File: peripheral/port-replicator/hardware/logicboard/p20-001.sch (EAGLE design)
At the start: 26 parts, among them IC11 74ALS04N, J0 DC9V, J11 AUDIO_JACK_3.5MM_PTH, J12 AUDIO_JACK_3.5MM_PTH, J13 AUDIO_JACK_3.5MM_PTH, J14 AUDIO_JACK_3.5MM_PTH, J7 DIN5, J8 DIN5, J9 DIN5, X0 MKDSN1,5/2-5,08

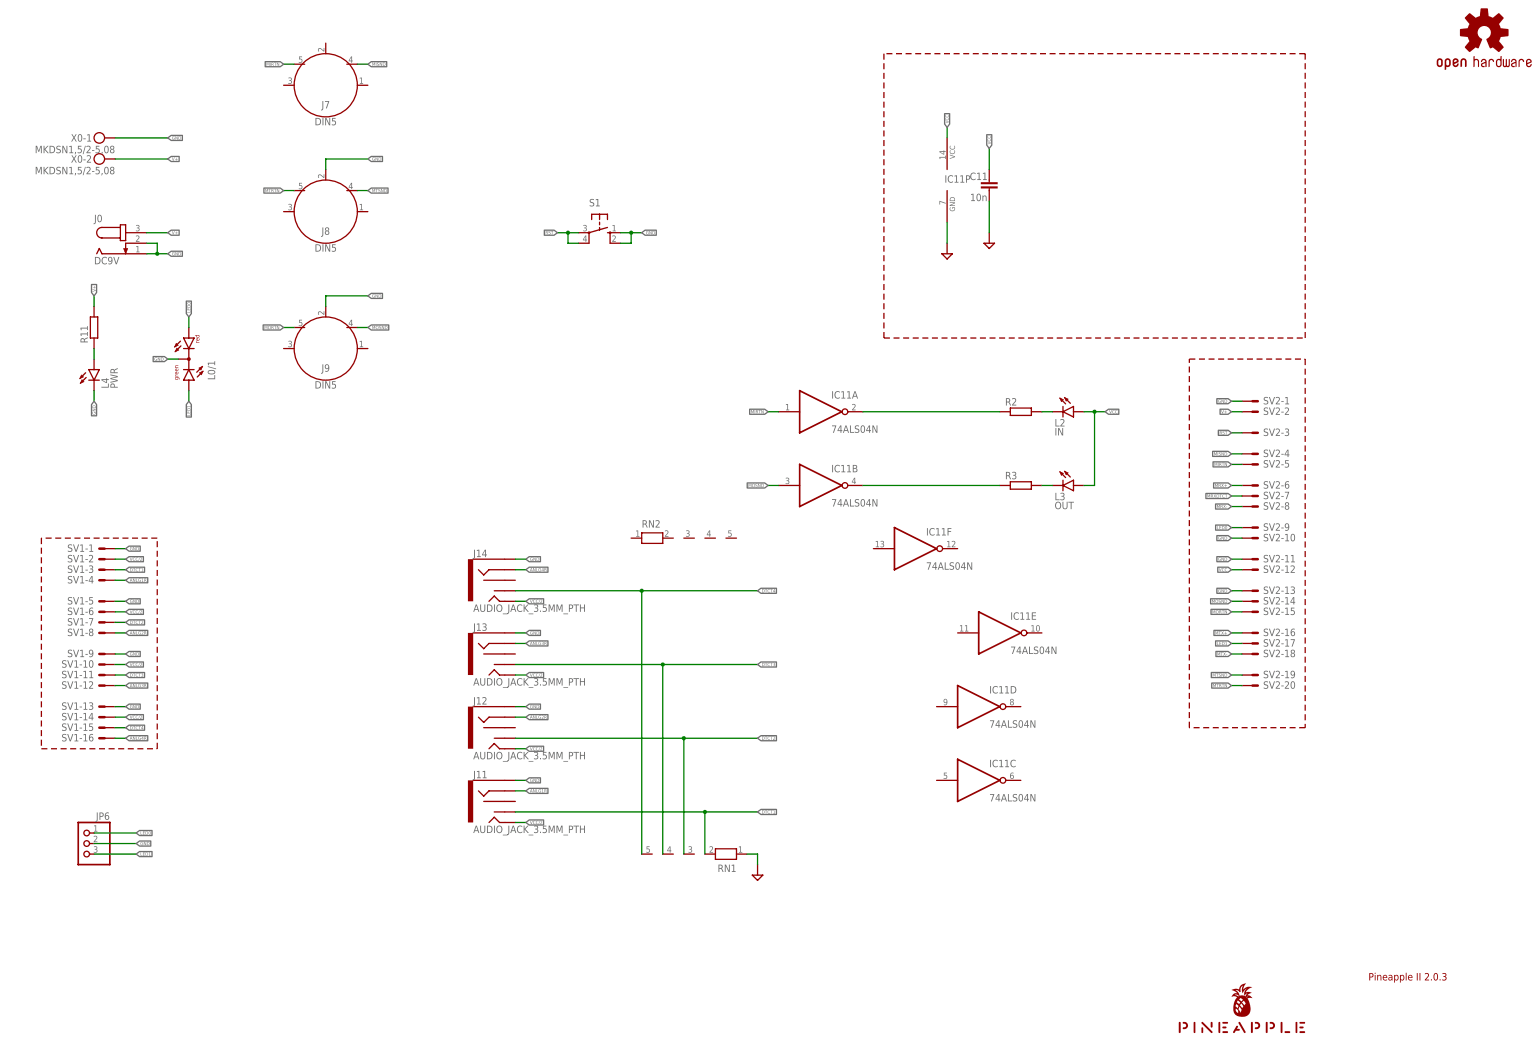
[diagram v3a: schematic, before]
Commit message: LED0->LED1, LED1->LED2, LED4->LED0.
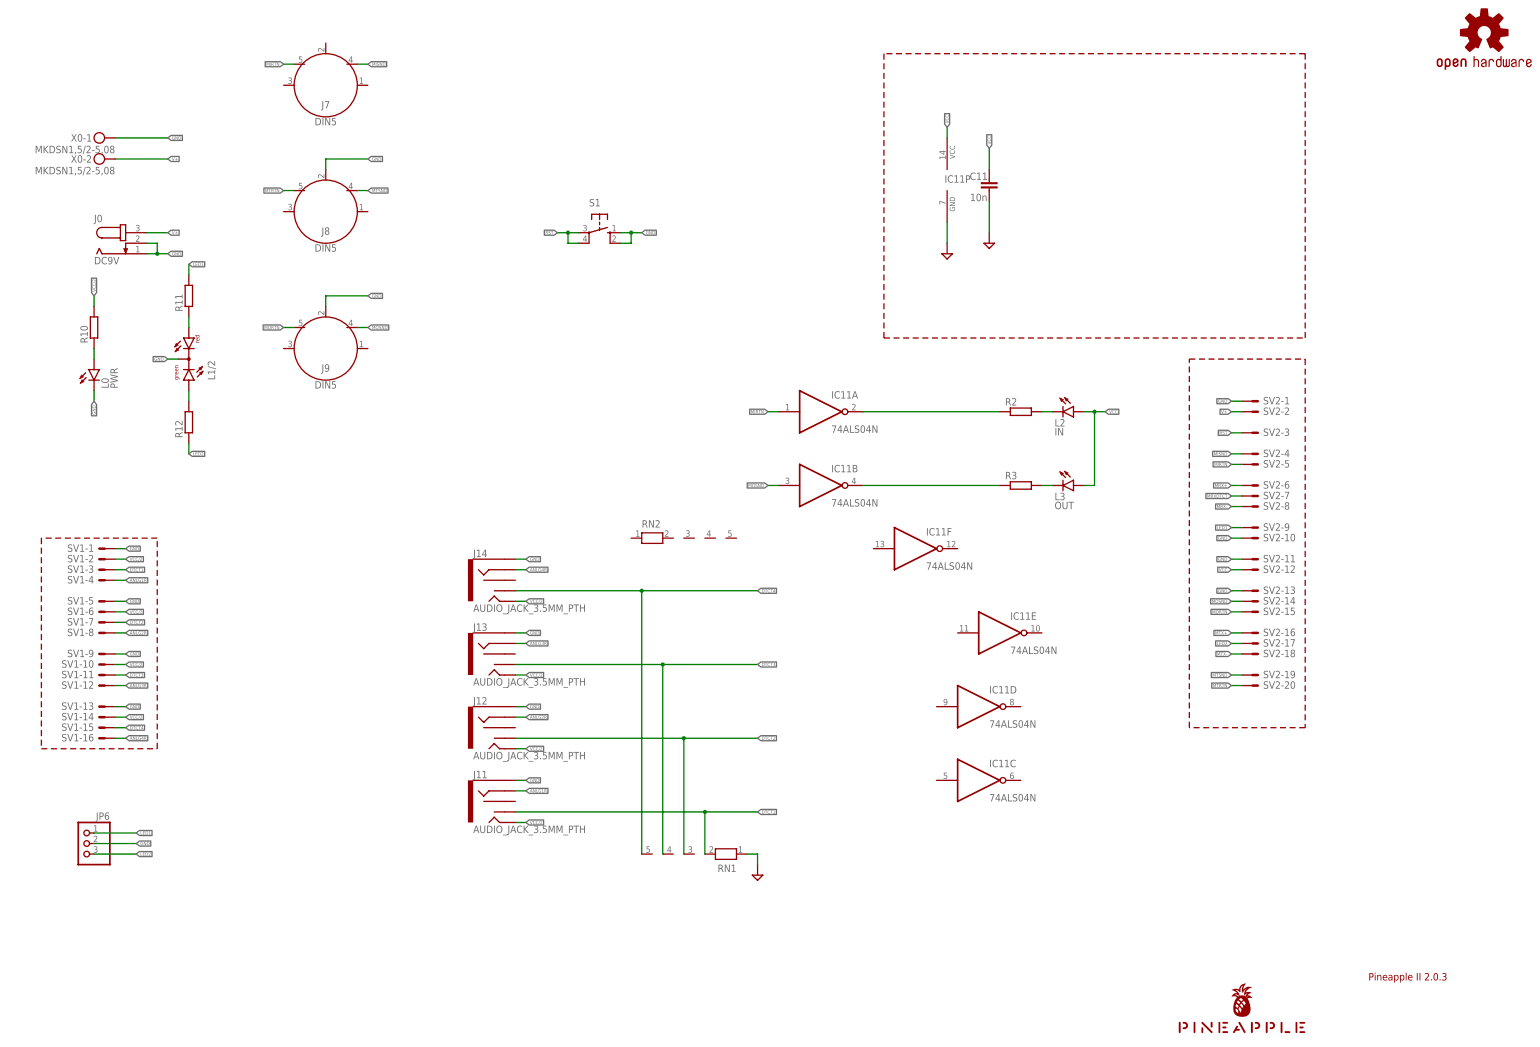
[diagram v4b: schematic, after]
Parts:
- added R10, R12: (no value), rcl:R-EU_0204/5
- renumbered L0/1 to L1/2, L4 to L0
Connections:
- removed net LED0: JP6.1, L1/2.AR, SV2-9.S
- new net LED2: JP6.3, R12.1, SV2-17.S
- new net N$3: L1/2.AR, R11.1
- new net N$5: L1/2.AG, R12.2
- net LED1: now also JP6.1, R11.2, SV2-9.S; no longer JP6.3, L1/2.AG, SV2-17.S
- net LEDPWR: now also R10.1; no longer R11.1
- net V+: no longer R11.2
- net VCC/2: now also R10.2
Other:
- moved on the sheet: R11
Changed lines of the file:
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@@
 <part name="J14" library="SparkFun-Connectors" library_urn="urn:adsk.eagle:library:513" deviceset="AUDIO_JACK_3.5MM" device="_PTH" package3d_urn="urn:adsk.eagle:package:37997/1"/>
 <part name="IC11" library="74xx-us" library_urn="urn:adsk.eagle:library:88" deviceset="74*04" device="N" package3d_urn="urn:adsk.eagle:package:16407/2" technology="ALS" value="74ALS04N"/>
-<part name="R11" library="rcl" library_urn="urn:adsk.eagle:library:334" deviceset="R-EU_" device="0204/5" package3d_urn="urn:adsk.eagle:package:23488/1"/>
+<part name="R10" library="rcl" library_urn="urn:adsk.eagle:library:334" deviceset="R-EU_" device="0204/5" package3d_urn="urn:adsk.eagle:package:23488/1"/>
 <part name="R2" library="rcl" library_urn="urn:adsk.eagle:library:334" deviceset="R-EU_" device="0204/5" package3d_urn="urn:adsk.eagle:package:23488/1"/>
-<part name="L4" library="led" library_urn="urn:adsk.eagle:library:259" deviceset="LED" device="3MM" package3d_urn="urn:adsk.eagle:package:15797/1" value="PWR"/>
+<part name="L0" library="led" library_urn="urn:adsk.eagle:library:259" deviceset="LED" device="3MM" package3d_urn="urn:adsk.eagle:package:15797/1" value="PWR"/>
 <part name="L2" library="led" library_urn="urn:adsk.eagle:library:259" deviceset="LED" device="3MM" package3d_urn="urn:adsk.eagle:package:15797/1" value="IN"/>
 <part name="L3" library="led" library_urn="urn:adsk.eagle:library:259" deviceset="LED" device="3MM" package3d_urn="urn:adsk.eagle:package:15797/1" value="OUT"/>
@@
 <part name="S1" library="switch-omron" library_urn="urn:adsk.eagle:library:377" deviceset="10-XX" device="" package3d_urn="urn:adsk.eagle:package:27496/1"/>
 <part name="JP6" library="pinhead" library_urn="urn:adsk.eagle:library:325" deviceset="PINHD-1X3" device="" package3d_urn="urn:adsk.eagle:package:22458/2"/>
-<part name="L0/1" library="led" library_urn="urn:adsk.eagle:library:259" deviceset="DUOLED-RG-C" device="" package3d_urn="urn:adsk.eagle:package:15851/1"/>
+<part name="L1/2" library="led" library_urn="urn:adsk.eagle:library:259" deviceset="DUOLED-RG-C" device="" package3d_urn="urn:adsk.eagle:package:15851/1"/>
 <part name="RN1" library="resistor-net" library_urn="urn:adsk.eagle:library:343" deviceset="RN04" device="" package3d_urn="urn:adsk.eagle:package:24976/1"/>
 <part name="SUPPLY2" library="supply2" deviceset="GND" device=""/>
 <part name="RN2" library="resistor-net" library_urn="urn:adsk.eagle:library:343" deviceset="RN04" device="" package3d_urn="urn:adsk.eagle:package:24976/1"/>
+<part name="R11" library="rcl" library_urn="urn:adsk.eagle:library:334" deviceset="R-EU_" device="0204/5" package3d_urn="urn:adsk.eagle:package:23488/1"/>
+<part name="R12" library="rcl" library_urn="urn:adsk.eagle:library:334" deviceset="R-EU_" device="0204/5" package3d_urn="urn:adsk.eagle:package:23488/1"/>
 </parts>
 <sheets>
@@
 <attribute name="VALUE" x="236.22" y="119.38" size="1.778" layer="96"/>
 </instance>
-<instance part="R11" gate="G$1" x="35.56" y="177.8" smashed="yes" rot="R90">
+<instance part="R10" gate="G$1" x="35.56" y="177.8" smashed="yes" rot="R90">
 <attribute name="NAME" x="34.0614" y="173.99" size="1.778" layer="95" rot="R90"/>
 <attribute name="VALUE" x="38.862" y="173.99" size="1.778" layer="96" rot="R90"/>
@@
 <attribute name="VALUE" x="255.27" y="154.178" size="1.778" layer="96"/>
 </instance>
-<instance part="L4" gate="G$1" x="35.56" y="167.64" smashed="yes">
+<instance part="L0" gate="G$1" x="35.56" y="167.64" smashed="yes">
 <attribute name="NAME" x="39.116" y="163.068" size="1.778" layer="95" rot="R90"/>
 <attribute name="VALUE" x="41.275" y="163.068" size="1.778" layer="96" rot="R90"/>
@@
 <attribute name="VALUE" x="39.37" y="45.72" size="1.778" layer="96" rot="MR0"/>
 </instance>
-<instance part="L0/1" gate="G$1" x="58.42" y="170.18" smashed="yes">
+<instance part="L1/2" gate="G$1" x="58.42" y="170.18" smashed="yes">
 <attribute name="NAME" x="64.77" y="165.1" size="1.778" layer="95" rot="R90"/>
 <attribute name="VALUE" x="67.31" y="165.1" size="1.778" layer="96" rot="R90"/>
@@
 <attribute name="NAME" x="167.64" y="129.54" size="1.778" layer="95"/>
 <attribute name="VALUE" x="167.64" y="122.682" size="1.778" layer="96"/>
+</instance>
+<instance part="R11" gate="G$1" x="58.42" y="185.42" smashed="yes" rot="R90">
+<attribute name="NAME" x="56.9214" y="181.61" size="1.778" layer="95" rot="R90"/>
+<attribute name="VALUE" x="61.722" y="181.61" size="1.778" layer="96" rot="R90"/>
+</instance>
+<instance part="R12" gate="G$1" x="58.42" y="154.94" smashed="yes" rot="R90">
+<attribute name="NAME" x="56.9214" y="151.13" size="1.778" layer="95" rot="R90"/>
+<attribute name="VALUE" x="61.722" y="151.13" size="1.778" layer="96" rot="R90"/>
 </instance>
 </instances>
@@
 </segment>
 <segment>
-<pinref part="L4" gate="G$1" pin="C"/>
+<pinref part="L0" gate="G$1" pin="C"/>
 <wire x1="35.56" y1="162.56" x2="35.56" y2="160.02" width="0.1524" layer="91"/>
 <label x="35.56" y="160.02" size="0.8128" layer="95" rot="R270" xref="yes"/>
@@
 </segment>
 <segment>
-<pinref part="L0/1" gate="G$1" pin="C"/>
+<pinref part="L1/2" gate="G$1" pin="C"/>
 <wire x1="55.88" y1="170.18" x2="53.34" y2="170.18" width="0.1524" layer="91"/>
 <label x="53.34" y="170.18" size="0.8128" layer="95" rot="R180" xref="yes"/>
@@
 <label x="139.7" y="111.76" size="0.8128" layer="95" xref="yes"/>
 </segment>
+<segment>
+<pinref part="R10" gate="G$1" pin="2"/>
+<wire x1="35.56" y1="185.42" x2="35.56" y2="182.88" width="0.1524" layer="91"/>
+<label x="35.56" y="185.42" size="0.8128" layer="95" rot="R90" xref="yes"/>
+</segment>
 </net>
 <net name="MISND" class="0">
@@
 </segment>
 <segment>
-<pinref part="R11" gate="G$1" pin="2"/>
-<wire x1="35.56" y1="185.42" x2="35.56" y2="182.88" width="0.1524" layer="91"/>
-<label x="35.56" y="185.42" size="0.8128" layer="95" rot="R90" xref="yes"/>
-</segment>
-<segment>
 <pinref part="X0" gate="-2" pin="KL"/>
 <wire x1="40.64" y1="218.44" x2="53.34" y2="218.44" width="0.1524" layer="91"/>
@@
 <net name="LEDPWR" class="0">
 <segment>
-<pinref part="R11" gate="G$1" pin="1"/>
-<pinref part="L4" gate="G$1" pin="A"/>
+<pinref part="R10" gate="G$1" pin="1"/>
+<pinref part="L0" gate="G$1" pin="A"/>
 <wire x1="35.56" y1="172.72" x2="35.56" y2="170.18" width="0.1524" layer="91"/>
 </segment>
 </net>
-<net name="LED0" class="0">
-<segment>
-<pinref part="L0/1" gate="G$1" pin="AR"/>
-<wire x1="58.42" y1="177.8" x2="58.42" y2="180.34" width="0.1524" layer="91"/>
-<label x="58.42" y="180.34" size="0.8128" layer="95" rot="R90" xref="yes"/>
-</segment>
+<net name="LED1" class="0">
 <segment>
 <pinref part="JP6" gate="A" pin="1"/>
@@
 <label x="309.88" y="129.54" size="0.8128" layer="95" rot="MR0" xref="yes"/>
 </segment>
-</net>
-<net name="LED1" class="0">
-<segment>
-<pinref part="L0/1" gate="G$1" pin="AG"/>
-<wire x1="58.42" y1="162.56" x2="58.42" y2="160.02" width="0.1524" layer="91"/>
-<label x="58.42" y="160.02" size="0.8128" layer="95" rot="R270" xref="yes"/>
-</segment>
+<segment>
+<pinref part="R11" gate="G$1" pin="2"/>
+<wire x1="58.42" y1="190.5" x2="58.42" y2="193.04" width="0.1524" layer="91"/>
+<label x="58.42" y="193.04" size="0.8128" layer="95" xref="yes"/>
+</segment>
+</net>
+<net name="LED2" class="0">
 <segment>
 <pinref part="JP6" gate="A" pin="3"/>
@@
 <label x="309.88" y="101.6" size="0.8128" layer="95" rot="MR0" xref="yes"/>
 </segment>
+<segment>
+<pinref part="R12" gate="G$1" pin="1"/>
+<wire x1="58.42" y1="149.86" x2="58.42" y2="147.32" width="0.1524" layer="91"/>
+<label x="58.42" y="147.32" size="0.8128" layer="95" xref="yes"/>
+</segment>
 </net>
 <net name="MRX+" class="0">
@@
 </segment>
 </net>
+<net name="N$3" class="0">
+<segment>
+<pinref part="L1/2" gate="G$1" pin="AR"/>
+<pinref part="R11" gate="G$1" pin="1"/>
+<wire x1="58.42" y1="177.8" x2="58.42" y2="180.34" width="0.1524" layer="91"/>
+</segment>
+</net>
+<net name="N$5" class="0">
+<segment>
+<pinref part="L1/2" gate="G$1" pin="AG"/>
+<pinref part="R12" gate="G$1" pin="2"/>
+<wire x1="58.42" y1="162.56" x2="58.42" y2="160.02" width="0.1524" layer="91"/>
+</segment>
+</net>
